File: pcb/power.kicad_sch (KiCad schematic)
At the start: 19 parts, among them J19 Conn_01x02_Pin, J20 Conn_01x02_Pin, J21 Conn_01x02_Pin, J22 Conn_01x02_Pin, J3 ATX-20, SW1 SW_SPDT, U3 AMS1117, U4 AMS1117

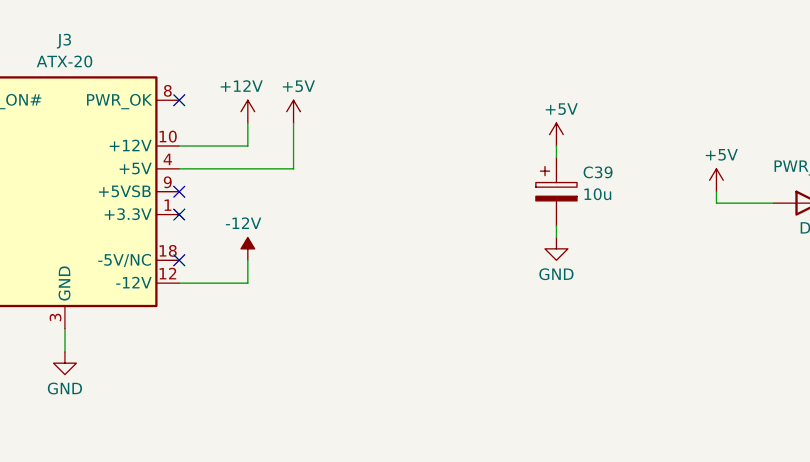
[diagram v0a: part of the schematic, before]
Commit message: use same 22uF cap for +5V rail, less part variance
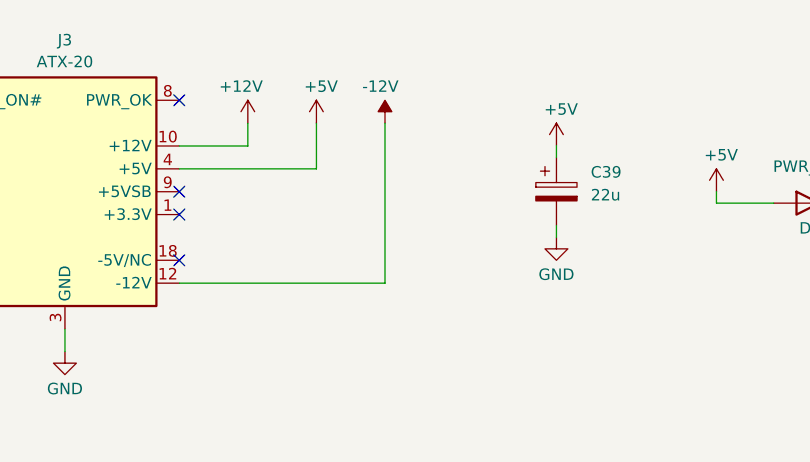
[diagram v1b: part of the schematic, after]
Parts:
- C39: value 10u -> 22u
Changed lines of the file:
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@@
 	(wire
 		(pts
-			(xy 96.52 59.69) (xy 109.22 59.69)
-		)
-		(stroke
-			(width 0)
-			(type default)
-		)
-	)
-	(wire
-		(pts
-			(xy 104.14 69.85) (xy 104.14 72.39)
+			(xy 96.52 59.69) (xy 111.76 59.69)
+		)
+		(stroke
+			(width 0)
+			(type default)
+		)
+	)
+	(wire
+		(pts
+			(xy 119.38 54.61) (xy 119.38 72.39)
 		)
 		(stroke
@@
 	(wire
 		(pts
-			(xy 109.22 59.69) (xy 109.22 54.61)
+			(xy 111.76 59.69) (xy 111.76 54.61)
 		)
 		(stroke
@@
 	(wire
 		(pts
-			(xy 96.52 72.39) (xy 104.14 72.39)
+			(xy 96.52 72.39) (xy 119.38 72.39)
 		)
 		(stroke
@@
 	(symbol
 		(lib_id "power:+5V")
-		(at 109.22 54.61 0)
+		(at 111.76 54.61 0)
 		(unit 1)
 		(exclude_from_sim no)
@@
 		(dnp no)
 		(property "Reference" "#PWR061"
-			(at 109.22 58.42 0)
+			(at 111.76 58.42 0)
 			(effects
 				(font
@@
 		)
 		(property "Value" "+5V"
-			(at 109.728 50.546 0)
+			(at 112.268 50.546 0)
 			(effects
 				(font
@@
 		)
 		(property "Footprint" ""
-			(at 109.22 54.61 0)
+			(at 111.76 54.61 0)
 			(effects
 				(font
@@
 		)
 		(property "Datasheet" ""
-			(at 109.22 54.61 0)
+			(at 111.76 54.61 0)
 			(effects
 				(font
@@
 		)
 		(property "Description" "Power symbol creates a global label with name \"+5V\""
-			(at 109.22 54.61 0)
+			(at 111.76 54.61 0)
 			(effects
 				(font
@@
 		(fields_autoplaced yes)
 		(property "Reference" "C39"
-			(at 141.351 60.1288 0)
+			(at 142.24 60.0709 0)
 			(effects
 				(font
@@
 			)
 		)
-		(property "Value" "10u"
-			(at 141.351 62.5531 0)
+		(property "Value" "22u"
+			(at 142.24 62.6109 0)
 			(effects
 				(font
@@
 	(symbol
 		(lib_id "power:-12V")
-		(at 104.14 69.85 0)
+		(at 119.38 54.61 0)
 		(unit 1)
 		(exclude_from_sim no)
@@
 		(dnp no)
 		(property "Reference" "#PWR063"
-			(at 104.14 73.66 0)
+			(at 119.38 58.42 0)
 			(effects
 				(font
@@
 		)
 		(property "Value" "-12V"
-			(at 103.632 65.786 0)
+			(at 118.872 50.546 0)
 			(effects
 				(font
@@
 		)
 		(property "Footprint" ""
-			(at 104.14 69.85 0)
+			(at 119.38 54.61 0)
 			(effects
 				(font
@@
 		)
 		(property "Datasheet" ""
-			(at 104.14 69.85 0)
+			(at 119.38 54.61 0)
 			(effects
 				(font
@@
 		)
 		(property "Description" "Power symbol creates a global label with name \"-12V\""
-			(at 104.14 69.85 0)
-			(effects
-				(font
+			(at 119.38 54.61 0)
+			(effects
+				(font

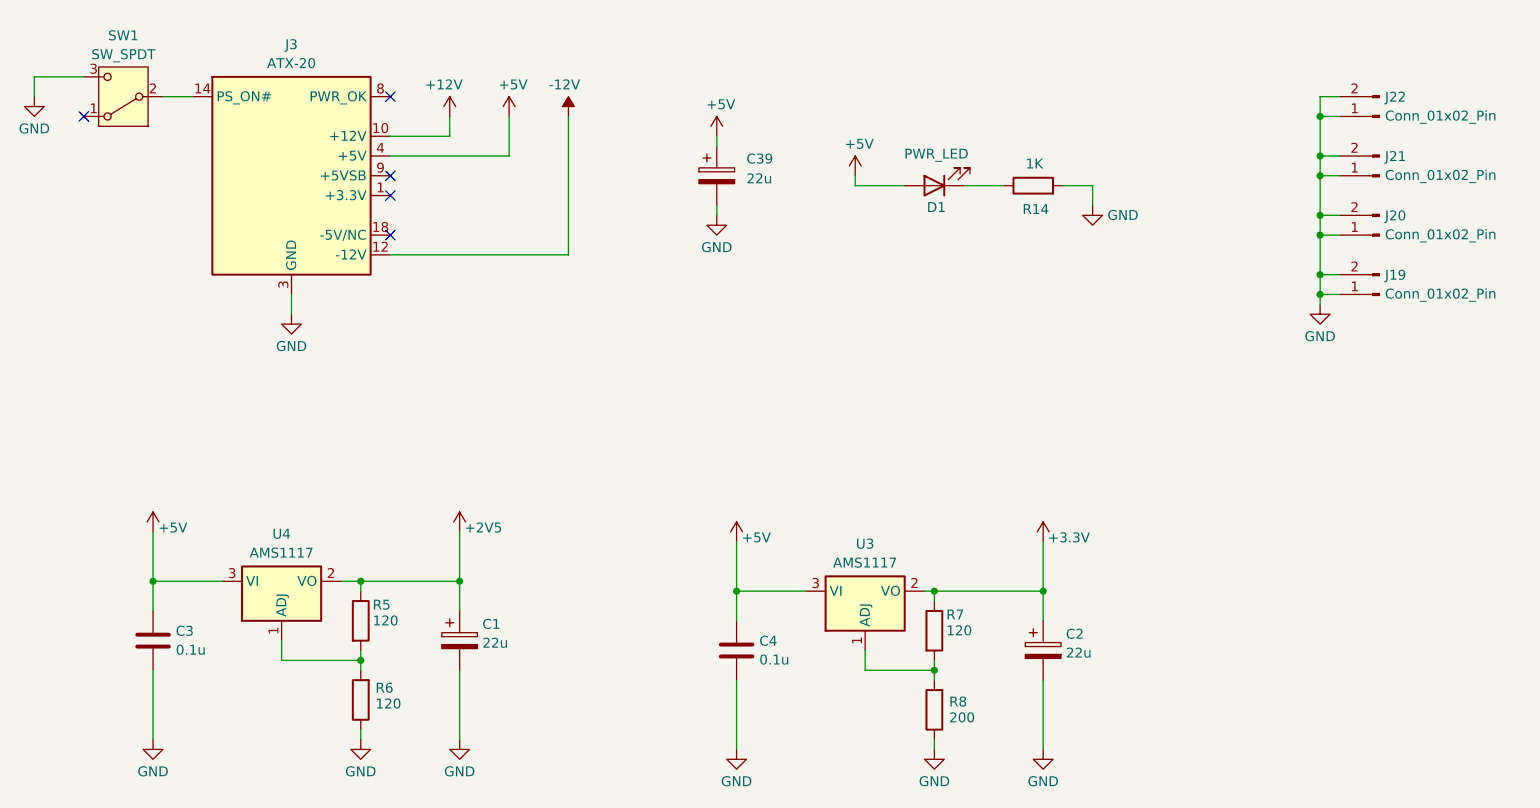
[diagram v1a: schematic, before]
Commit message: power diagram aligned, added option to use ATX 3.3V instead of populating U3
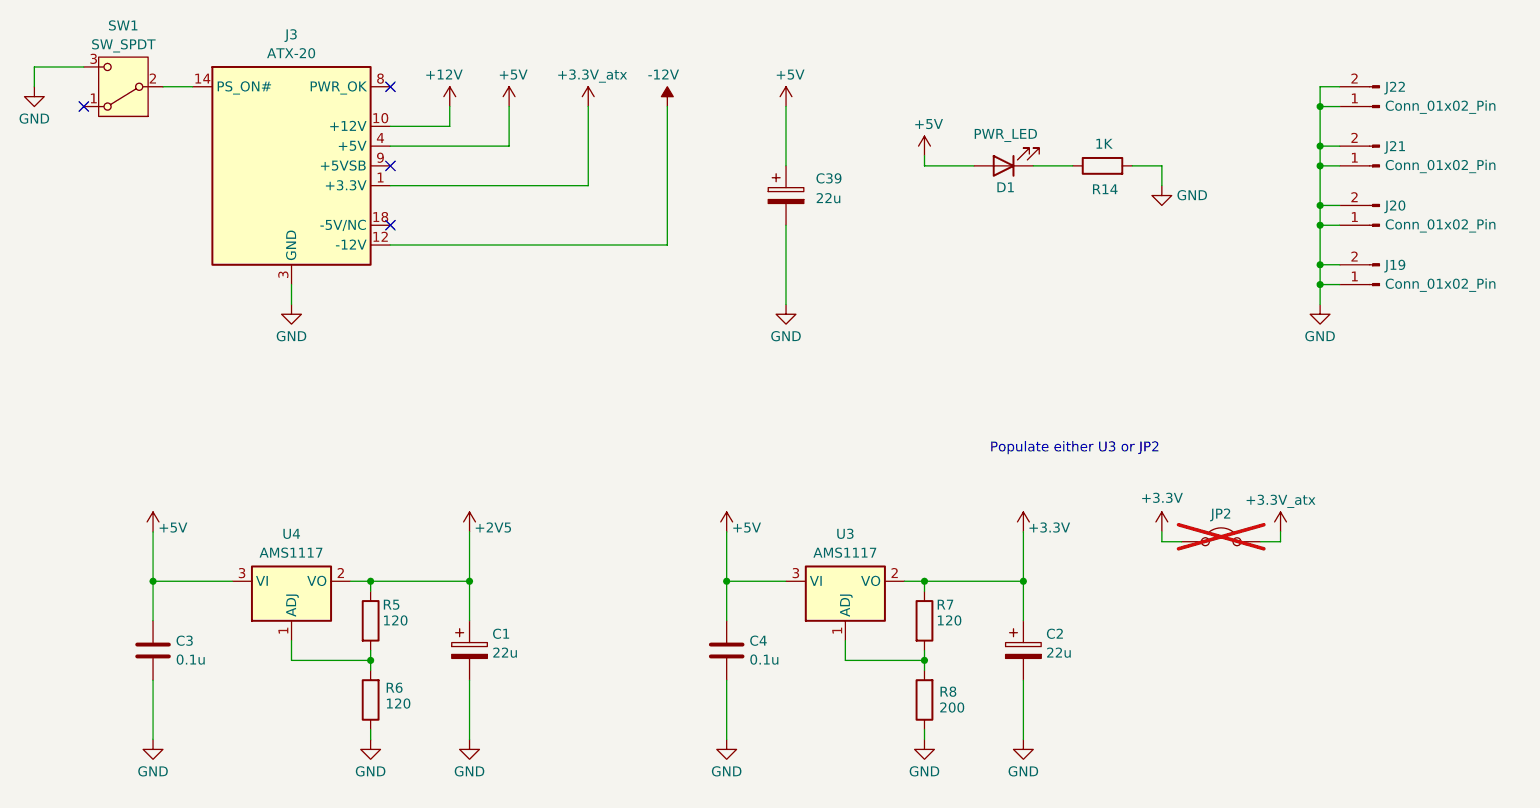
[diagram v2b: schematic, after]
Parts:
- added JP2: Jumper_2_Open, Fuse:Fuse_1210_3225Metric, symbol Jumper:Jumper_2_Open
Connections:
- net +3.3V: now also JP2.1 (A)
- net +3.3V_atx: now reaches J3.1 (+3.3V), J3.11 (+3.3V), J3.2 (+3.3V)
- net +3.3V_atx: now also JP2.2 (B)
- no-connect marks 5 -> 4
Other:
- note added: "Populate either U3 or JP2"
- moved on the sheet: C1, C2, C3, C39, C4, D1, J19, J20, J21, J22, J3, R14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

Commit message: atx jumper label
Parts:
- JP2: value Jumper_2_Open -> ATX power
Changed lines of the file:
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@@
 			)
 		)
-		(property "Value" "Jumper_2_Open"
+		(property "Value" "ATX power"
 			(at 203.2 105.41 0)
 			(effects
